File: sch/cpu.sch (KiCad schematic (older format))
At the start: 28 parts

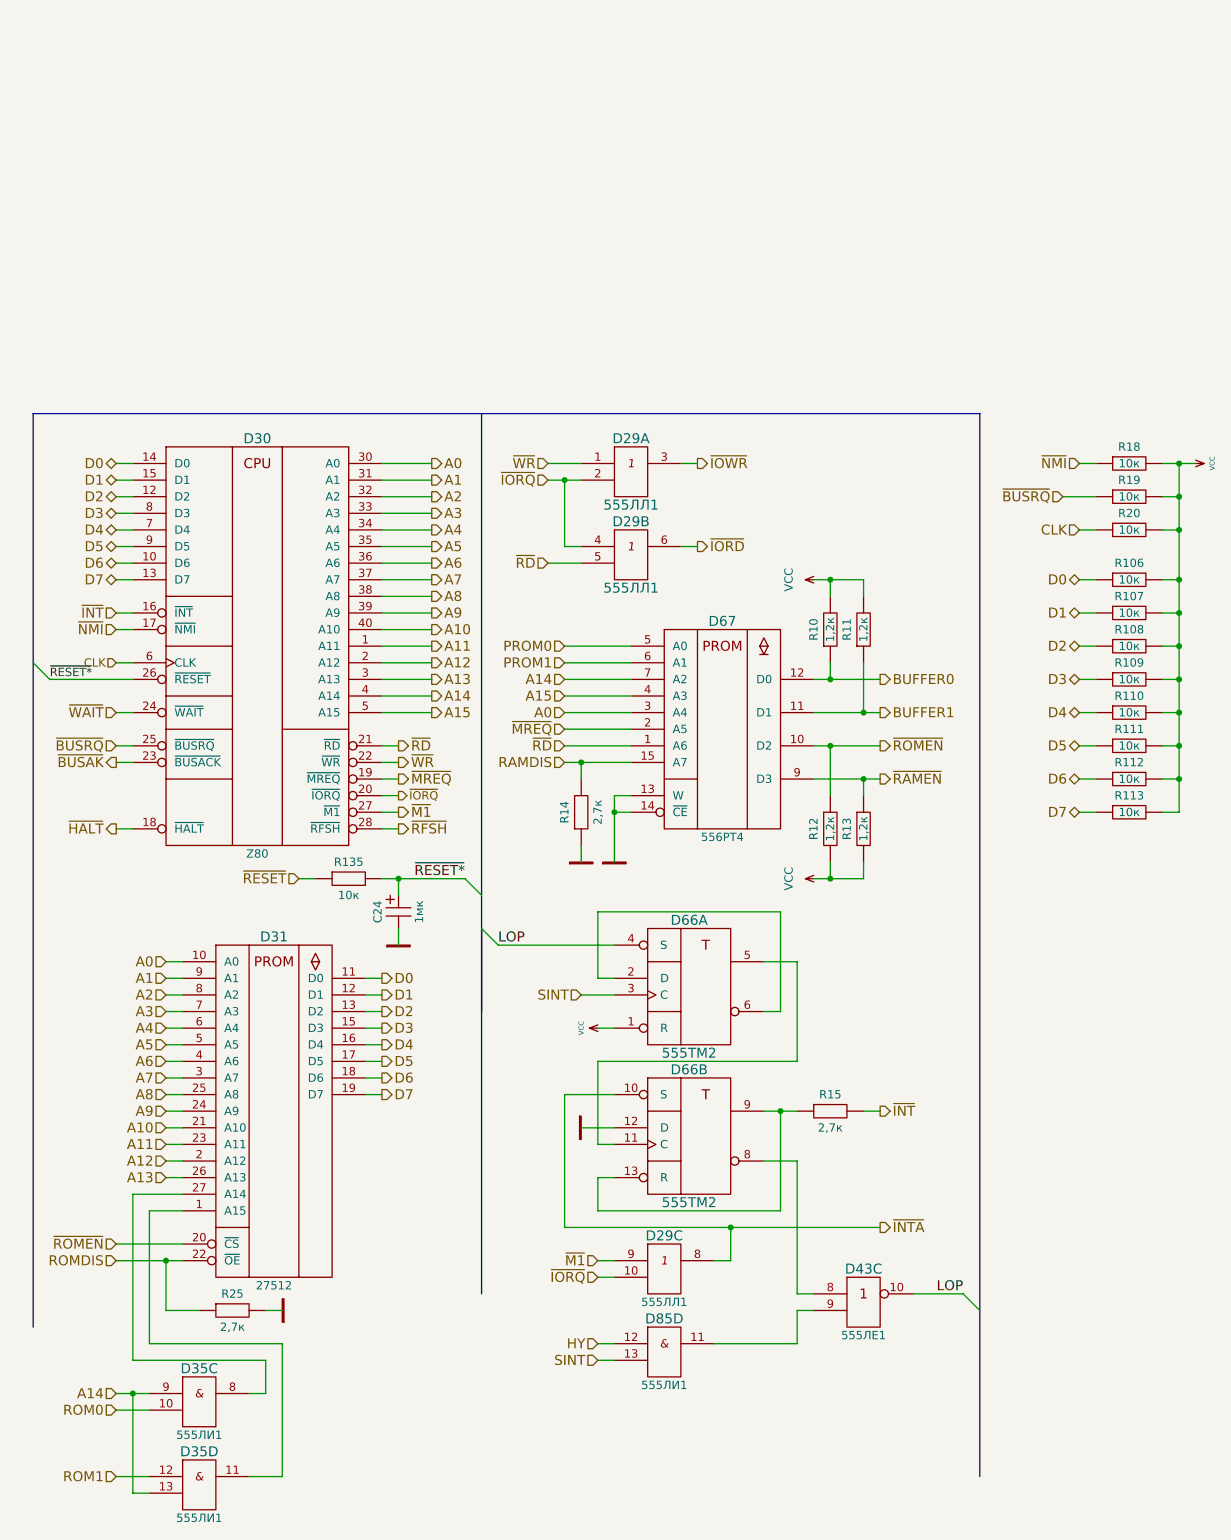
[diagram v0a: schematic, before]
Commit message: Start to move to a bit more affordable components
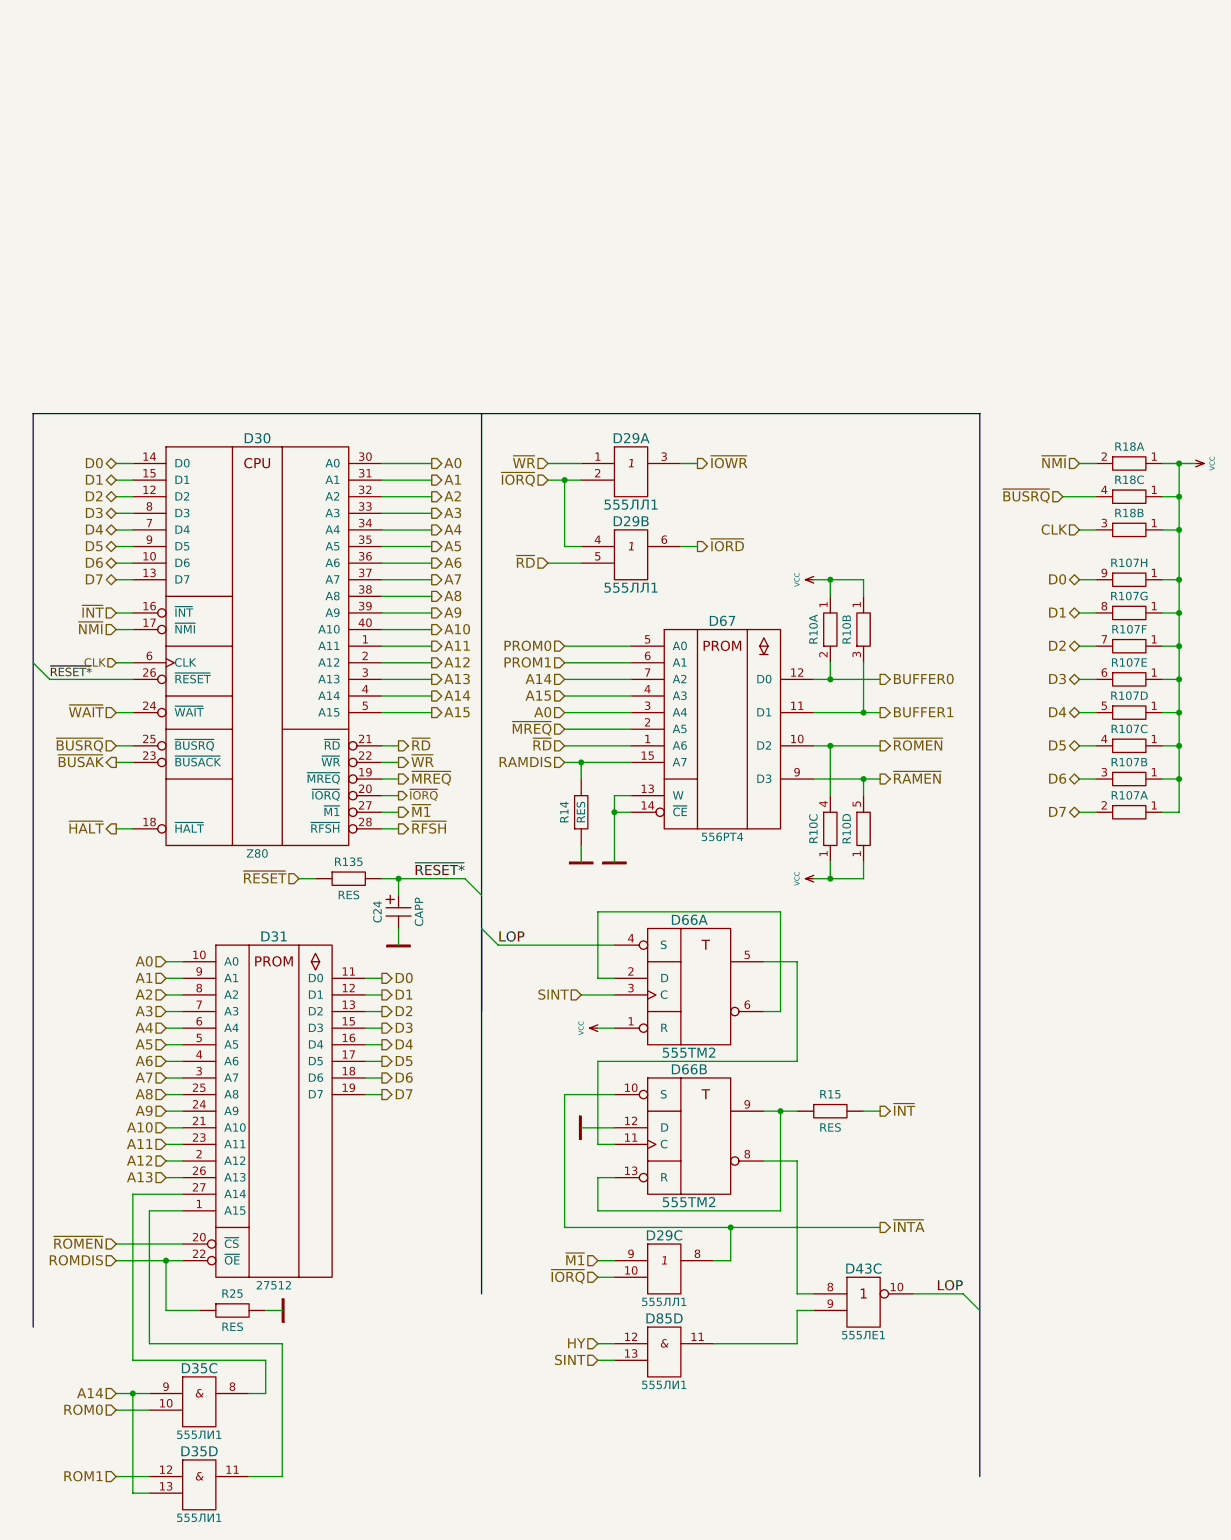
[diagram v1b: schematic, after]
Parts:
- removed R10, R11, R12, R13: 1,2к, MyLib:Resistor_Vertical_RM2.5mm, symbol RES
- removed R106, R107, R108, R109, R110, R111, R112, R113, R18, R19, R20: 10к, MyLib:Resistor_Vertical_RM2.5mm, symbol RES
- added R10: RES_PACK4_C, MyLib:Resistor_Array_SIP4, symbol RES_PACK4_C
- added R107: RES_PACK8_C, Resistors_ThroughHole:Resistor_Array_SIP8, symbol RES_PACK8_C
- added R18: RES_PACK4_C, MyLib:Resistor_Array_SIP3, symbol RES_PACK4_C
- C24: value 1мк -> CAPP
- R135: value 10к -> RES
- R14, R15, R25: value 2,7к -> RES
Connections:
- net BUFFER0: now also R10.2
- net BUFFER1: now also R10.3
- net CLK: now also R18.3
- net D0: now also R107.9
- net D1: now also R107.8
- net D2: now also R107.7
- net D3: now also R107.6
- net D4: now also R107.5
- net D5: now also R107.4
- net D6: now also R107.3
- net D7: now also R107.2
- net VCC: now also R10.1, R10.1, R10.1, R10.1, R107.1, R107.1, R107.1, R107.1, R107.1, R107.1, R107.1, R107.1, R18.1, R18.1, R18.1
- net ~BUSRQ: now also R18.4
- net ~NMI: now also R18.2
- net ~RAMEN: now also R10.5
- net ~ROMEN: now also R10.4

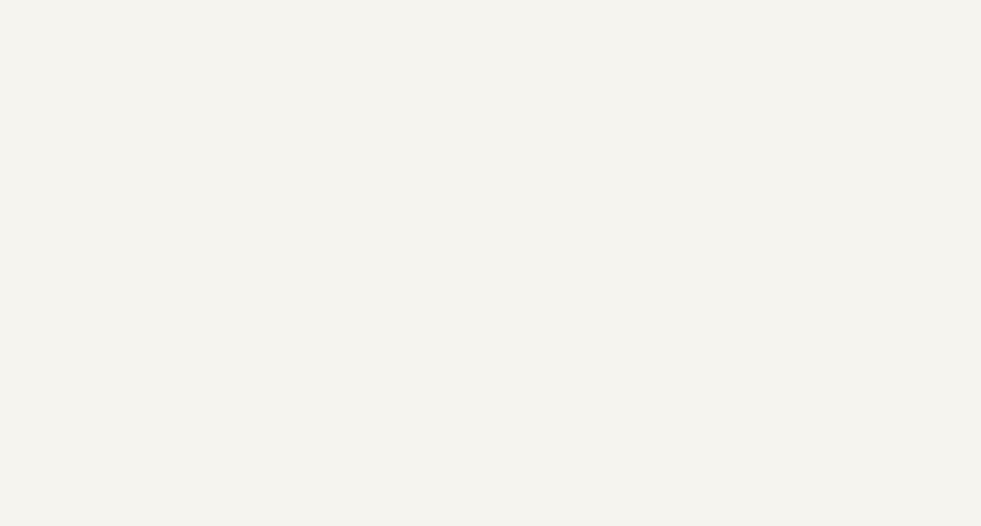
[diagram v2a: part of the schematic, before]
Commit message: Fix MVI signal
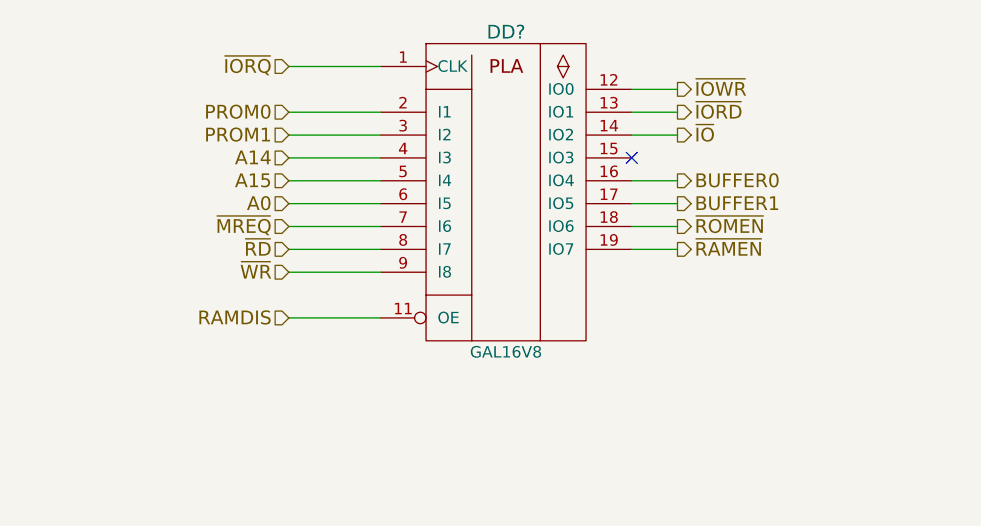
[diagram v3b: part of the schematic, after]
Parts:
- added DD?: GAL16V8, symbol GAL16V8
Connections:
- net A0: now also DD?.6 (I5)
- net A14: now also DD?.4 (I3)
- net A15: now also DD?.5 (I4)
- net BUFFER0: now also DD?.16 (IO4)
- net BUFFER1: now also DD?.17 (IO5)
- net GND: now also DD?.10 (GND)
- net PROM0: now also DD?.2 (I1)
- net PROM1: now also DD?.3 (I2)
- net RAMDIS: now also DD?.11 (OE)
- net VCC: now also DD?.20 (VCC)
- net ~IORD: now also DD?.13 (IO1)
- net ~IORQ: now also DD?.1 (CLK)
- net ~IOWR: now also DD?.12 (IO0)
- net ~MREQ: now also DD?.7 (I6)
- net ~RAMEN: now also DD?.19 (IO7)
- net ~RD: now also DD?.8 (I7)
- net ~ROMEN: now also DD?.18 (IO6)
- net ~WR: now also DD?.9 (I8)
- new net ~IO: DD?.14 (IO2)
- no-connect marks 0 -> 1
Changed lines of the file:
@@
 	1    0    0    -1
 $EndComp
+$Comp
+L GAL16V8 DD?
+U 1 1 57CC105B
+P 4000 -1600
+F 0 "DD?" H 4550 -1450 60  0000 C CNN
+F 1 "GAL16V8" H 4550 -2850 50  0000 C CNN
+F 2 "" H 4300 -1850 60  0000 C CNN
+F 3 "" H 4300 -1850 60  0000 C CNN
+	1    4000 -1600
+	1    0    0    -1
+$EndComp
+Text HLabel 3600 -1400 0    60   Input ~ 0
+PROM0
+Text HLabel 3600 -1300 0    60   Input ~ 0
+PROM1
+Text HLabel 3600 -1200 0    60   Input ~ 0
+A14
+Text HLabel 3600 -1100 0    60   Input ~ 0
+A15
+Text HLabel 3600 -1000 0    60   Input ~ 0
+A0
+Text HLabel 3600 -900 0    60   Input ~ 0
+~MREQ
+Wire Wire Line
+	3600 -900 4000 -900
+Text HLabel 3600 -800 0    60   Input ~ 0
+~RD
+Wire Wire Line
+	3600 -800 4000 -800
+Text HLabel 3600 -500 0    60   Input ~ 0
+RAMDIS
+Wire Wire Line
+	3600 -700 4000 -700
+Wire Wire Line
+	3600 -1000 4000 -1000
+Wire Wire Line
+	3600 -1100 4000 -1100
+Wire Wire Line
+	3600 -1200 4000 -1200
+Wire Wire Line
+	3600 -1300 4000 -1300
+Wire Wire Line
+	3600 -1400 4000 -1400
+Text HLabel 5300 -800 2    60   Output ~ 0
+~RAMEN
+Text HLabel 5300 -1000 2    60   Output ~ 0
+BUFFER1
+Text HLabel 5300 -1100 2    60   Output ~ 0
+BUFFER0
+Text HLabel 5300 -900 2    60   Output ~ 0
+~ROMEN
+Wire Wire Line
+	5300 -800 5100 -800
+Wire Wire Line
+	5300 -1100 5100 -1100
+Wire Wire Line
+	5300 -1000 5100 -1000
+Wire Wire Line
+	5100 -900 5300 -900
+Text HLabel 3600 -1600 0    60   Input ~ 0
+~IORQ
+Wire Wire Line
+	3600 -1600 4000 -1600
+Wire Wire Line
+	3600 -500 4000 -500
+Text HLabel 3600 -700 0    60   Input ~ 0
+~WR
+Text HLabel 5300 -1500 2    60   Output ~ 0
+~IOWR
+Text HLabel 5300 -1400 2    60   Output ~ 0
+~IORD
+Text HLabel 5300 -1300 2    60   Output ~ 0
+~IO
+Wire Wire Line
+	5300 -1300 5100 -1300
+Wire Wire Line
+	5100 -1400 5300 -1400
+Wire Wire Line
+	5300 -1500 5100 -1500
+NoConn ~ 5100 -1200
 $EndSCHEMATC
